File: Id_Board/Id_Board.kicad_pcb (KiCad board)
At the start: 2 copper layers, 130 x 50 mm, 2 parts

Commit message: finished IdBoard
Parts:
- removed REF1: RJ45_Amphenol_RJHSE5380-08, Connector_RJ:RJ45_Amphenol_RJHSE5380-08
- removed REF2: SW_DIP_SPSTx07_Slide_9.78x19.96mm_W7.62mm_P2.54mm, Button_Switch_THT:SW_DIP_SPSTx07_Slide_9.78x19.96mm_W7.62mm_P2.54mm
- added H1: MountingHole, MountingHole:MountingHole_3.2mm_M3, F.Cu at (64.5, 60.0)
- added H2: MountingHole, MountingHole:MountingHole_3.2mm_M3, F.Cu at (175.5, 60.0)
- added H3: MountingHole, MountingHole:MountingHole_3.2mm_M3, F.Cu at (100.0, 70.0)
- added H4: MountingHole, MountingHole:MountingHole_3.2mm_M3, F.Cu at (140.0, 70.0)
- added J1: ~, LCSC:RJ45-TH_HC-WK88-H13-1X8-55QS_1, F.Cu at (120.0, 48.0)
- added J2: Conn_01x02_Pin, Connector_JST:JST_PH_B2B-PH-SM4-TB_1x02-1MP_P2.00mm_Vertical, F.Cu at (74.4, 65.6)
- added J3: Conn_01x02_Pin, Connector_JST:JST_PH_B2B-PH-SM4-TB_1x02-1MP_P2.00mm_Vertical, F.Cu at (164.9, 66.1)
- added R1: 0, Resistor_SMD:R_0603_1608Metric, F.Cu at (163.1, 53.5)
- added R10: 0, Resistor_SMD:R_0603_1608Metric, F.Cu at (121.0, 53.5)
- added R11: 0, Resistor_SMD:R_0603_1608Metric, F.Cu at (124.5, 53.5)
- added R12: 0, Resistor_SMD:R_0603_1608Metric, F.Cu at (122.8, 53.5)
- added R13: 0, Resistor_SMD:R_0603_1608Metric, F.Cu at (107.0, 53.5)
- added R14: 0, Resistor_SMD:R_0603_1608Metric, F.Cu at (110.5, 53.5)
- added R15: 0, Resistor_SMD:R_0603_1608Metric, F.Cu at (108.8, 53.5)
- added R16: 0, Resistor_SMD:R_0603_1608Metric, F.Cu at (93.1, 53.5)
- added R17: 0, Resistor_SMD:R_0603_1608Metric, F.Cu at (96.5, 53.5)
- added R18: 0, Resistor_SMD:R_0603_1608Metric, F.Cu at (94.8, 53.5)
- added R19: 0, Resistor_SMD:R_0603_1608Metric, F.Cu at (79.0, 53.5)
- added R2: 0, Resistor_SMD:R_0603_1608Metric, F.Cu at (166.5, 53.5)
- added R20: 0, Resistor_SMD:R_0603_1608Metric, F.Cu at (82.5, 53.5)
- added R21: 0, Resistor_SMD:R_0603_1608Metric, F.Cu at (80.8, 53.5)
- added R22: 0, Resistor_SMD:R_0603_1608Metric, F.Cu at (64.6, 53.5)
- added R23: 0, Resistor_SMD:R_0603_1608Metric, F.Cu at (68.5, 53.5)
- added R24: 0, Resistor_SMD:R_0603_1608Metric, F.Cu at (66.6, 53.5)
- added R3: 0, Resistor_SMD:R_0603_1608Metric, F.Cu at (164.8, 53.5)
- added R4: 0, Resistor_SMD:R_0603_1608Metric, F.Cu at (149.0, 53.5)
- added R5: 0, Resistor_SMD:R_0603_1608Metric, F.Cu at (152.5, 53.5)
- added R6: 0, Resistor_SMD:R_0603_1608Metric, F.Cu at (150.8, 53.5)
- added R7: 0, Resistor_SMD:R_0603_1608Metric, F.Cu at (135.0, 53.5)
- added R8: 0, Resistor_SMD:R_0603_1608Metric, F.Cu at (138.5, 53.5)
- added R9: 0, Resistor_SMD:R_0603_1608Metric, F.Cu at (136.8, 53.5)
- added SW1: SW_DIP_x08, LCSC:SW-SMD_16P-L20.3-W6.0-P2.54-LS9.3-BL, F.Cu at (120.0, 66.5)
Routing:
- net BoardA: track 0.00 -> 178.6 mm, vias 0 -> 7
- net BoardC: track 0.00 -> 170.7 mm, vias 0 -> 9
- net BoardB: track 0.00 -> 159.8 mm, vias 0 -> 9
- net BoardD: track 0.00 -> 143.2 mm, vias 0 -> 1
- net ParityB: track 0.00 -> 118.5 mm, vias 0 -> 5
- net ParityA: track 0.00 -> 112.7 mm, vias 0 -> 4
- net GND: track 0.00 -> 52.6 mm, vias 0 -> 8
- net Net-(J1-PadE3): track 0.00 -> 7.27 mm
- net Net-(J1-PadC3): track 0.00 -> 7.17 mm
- net Net-(J1-PadH1): track 0.00 -> 7.11 mm
- net Net-(J1-PadH3): track 0.00 -> 7.10 mm
- net Net-(J1-PadF3): track 0.00 -> 7.04 mm
- net Net-(J1-PadD3): track 0.00 -> 7.04 mm
- net Net-(J1-PadB3): track 0.00 -> 7.04 mm
- net Net-(J1-PadA3): track 0.00 -> 7.02 mm
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- added copper zone on B.Cu, net GND
- added copper zone on F.Cu, net GND
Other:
- board size 130 x 50 mm -> 120 x 35 mm

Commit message: Production File generate
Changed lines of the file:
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@@
 				(font
 					(size 1.27 1.27)
+					(thickness 0.15)
 				)
 			)
@@
 				(font
 					(size 1.27 1.27)
+					(thickness 0.15)
 				)
 			)
@@
 				(font
 					(size 1.27 1.27)
+					(thickness 0.15)
 				)
 			)
@@
 		(sheetname "/")
 		(sheetfile "Id_Board.kicad_sch")
-		(units
-			(unit
-				(name "A")
-				(pins "A8" "A7" "A6" "A5" "A4" "A3" "A2" "A1")
-			)
-			(unit
-				(name "B")
-				(pins "B8" "B7" "B6" "B5" "B4" "B3" "B2" "B1")
-			)
-			(unit
-				(name "C")
-				(pins "C8" "C7" "C6" "C5" "C4" "C3" "C2" "C1")
-			)
-			(unit
-				(name "D")
-				(pins "D8" "D7" "D6" "D5" "D4" "D3" "D2" "D1")
-			)
-			(unit
-				(name "E")
-				(pins "E8" "E7" "E6" "E5" "E4" "E3" "E2" "E1")
-			)
-			(unit
-				(name "F")
-				(pins "F8" "F7" "F6" "F5" "F4" "F3" "F2" "F1")
-			)
-			(unit
-				(name "G")
-				(pins "G8" "G7" "G6" "G5" "G4" "G3" "G2" "G1")
-			)
-			(unit
-				(name "H")
-				(pins "H8" "H7" "H6" "H5" "H4" "H3" "H2" "H1")
-			)
-		)
 		(attr through_hole)
 		(duplicate_pad_numbers_are_jumpers no)
@@
 			)
 		)
-		(pad "" thru_hole circle
+		(pad "" np_thru_hole circle
 			(at -54.75 3.86 180)
 			(size 3.2 3.2)
 			(drill 3.2)
 			(layers "*.Cu" "*.Mask")
-			(remove_unused_layers no)
 		)
-		(pad "" thru_hole circle
+		(pad "" np_thru_hole circle
 			(at 54.75 3.86 180)
 			(size 3.2 3.2)
 			(drill 3.2)
 			(layers "*.Cu" "*.Mask")
-			(remove_unused_layers no)
 		)
 		(pad "A1" thru_hole circle
@@
 				(font
 					(size 1.27 1.27)
+					(thickness 0.15)
 				)
 			)
@@
 				(font
 					(size 1.27 1.27)
+					(thickness 0.15)
 				)
 			)
@@
 				(font
 					(size 1.27 1.27)
+					(thickness 0.15)
 				)
 			)
@@
 				(font
 					(size 1.27 1.27)
+					(thickness 0.15)
 				)
 			)
@@
 				(font
 					(size 1.27 1.27)
+					(thickness 0.15)
 				)
 			)
@@
 				(font
 					(size 1.27 1.27)
+					(thickness 0.15)
 				)
 			)
@@
 				(font
 					(size 1.27 1.27)
+					(thickness 0.15)
 				)
 			)
@@
 				(font
 					(size 1.27 1.27)
+					(thickness 0.15)
 				)
 			)
@@
 				(font
 					(size 1.27 1.27)
+					(thickness 0.15)
 				)
 			)
@@
 				(font
 					(size 1.27 1.27)
+					(thickness 0.15)
 				)
 			)
@@
 				(font
 					(size 1.27 1.27)
+					(thickness 0.15)
 				)
 			)
@@
 				(font
 					(size 1.27 1.27)
+					(thickness 0.15)
 				)
 			)
@@
 				(font
 					(size 1.27 1.27)
+					(thickness 0.15)
 				)
 			)
@@
 				(font
 					(size 1.27 1.27)
+					(thickness 0.15)
 				)
 			)
@@
 				(font
 					(size 1.27 1.27)
+					(thickness 0.15)
 				)
 			)
@@
 				(font
 					(size 1.27 1.27)
+					(thickness 0.15)
 				)
 			)
@@
 				(font
 					(size 1.27 1.27)
+					(thickness 0.15)
 				)
 			)
@@
 				(font
 					(size 1.27 1.27)
+					(thickness 0.15)
 				)
 			)
@@
 				(font
 					(size 1.27 1.27)
+					(thickness 0.15)
 				)
 			)
@@
 				(font
 					(size 1.27 1.27)
+					(thickness 0.15)
 				)
 			)
@@
 				(font
 					(size 1.27 1.27)
+					(thickness 0.15)
 				)
 			)

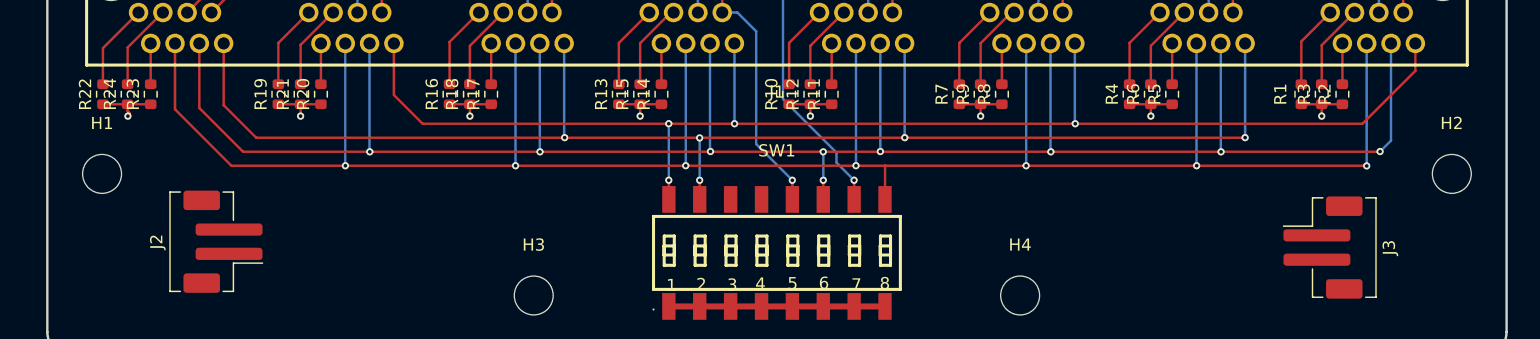
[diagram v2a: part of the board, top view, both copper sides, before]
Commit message: prettify silkscreen
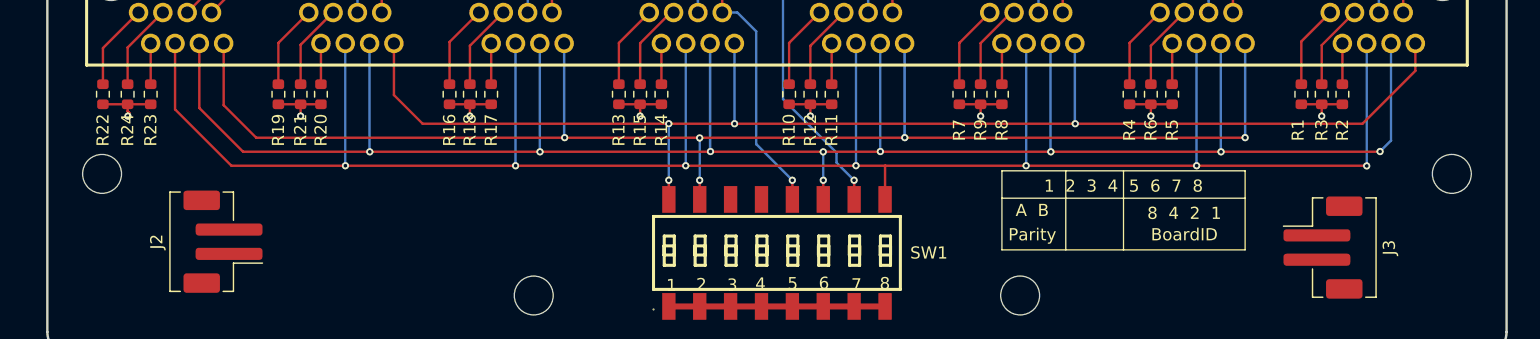
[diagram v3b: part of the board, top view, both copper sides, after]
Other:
- board text added: "1 2 3 4 5 6 7 8"
- board text added: "8 4 2 1"
- board text added: "A B"
- board text added: "BoardID"
- board text added: "Parity"
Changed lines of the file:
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@@
 		(tags "resistor")
 		(property "Reference" "R22"
-			(at 0 -1.43 90)
+			(at -2.95 0 90)
 			(layer "F.SilkS")
 			(effects
@@
 		(tags "resistor")
 		(property "Reference" "R24"
-			(at 0 -1.43 90)
+			(at -2.95 0 90)
 			(layer "F.SilkS")
 			(effects
@@
 		(tags "resistor")
 		(property "Reference" "R17"
-			(at 0 -1.43 90)
+			(at -2.95 0 90)
 			(layer "F.SilkS")
 			(effects
@@
 			(at 0 -4.15 0)
 			(layer "F.SilkS")
+			(hide yes)
 			(effects
 				(font
@@
 			(at 0 -5.27 0)
 			(layer "F.SilkS")
+			(hide yes)
 			(effects
 				(font
@@
 		(tags "resistor")
 		(property "Reference" "R15"
-			(at 0 -1.43 90)
+			(at -2.95 0 90)
 			(layer "F.SilkS")
 			(effects
@@
 		(tags "resistor")
 		(property "Reference" "R18"
-			(at 0 -1.43 90)
+			(at -2.95 0 90)
 			(layer "F.SilkS")
 			(effects
@@
 		(tags "resistor")
 		(property "Reference" "R19"
-			(at 0 -1.43 90)
+			(at -2.95 0 90)
 			(layer "F.SilkS")
 			(effects
@@
 			(at 0 -4.15 0)
 			(layer "F.SilkS")
+			(hide yes)
 			(effects
 				(font
@@
 			(at 0 -4.15 0)
 			(layer "F.SilkS")
+			(hide yes)
 			(effects
 				(font
@@
 		(tags "resistor")
 		(property "Reference" "R14"
-			(at 0 -1.43 90)
+			(at -2.95 0 90)
 			(layer "F.SilkS")
 			(effects
@@
 		(tags "resistor")
 		(property "Reference" "R2"
-			(at 0 -1.43 90)
+			(at -2.95 0 90)
 			(layer "F.SilkS")
 			(effects
@@
 		(tags "resistor")
 		(property "Reference" "R20"
-			(at 0 -1.43 90)
+			(at -2.95 0 90)
 			(layer "F.SilkS")
 			(effects
@@
 		(tags "resistor")
 		(property "Reference" "R10"
-			(at 0 -1.43 90)
+			(at -2.95 0 90)
 			(layer "F.SilkS")
 			(effects
@@
 		(tags "resistor")
 		(property "Reference" "R11"
-			(at 0 -1.43 90)
+			(at -2.95 0 90)
 			(layer "F.SilkS")
 			(effects
@@
 		(tags "resistor")
 		(property "Reference" "R23"
-			(at 0 -1.43 90)
+			(at -2.95 0 90)
 			(layer "F.SilkS")
 			(effects
@@
 		(tags "resistor")
 		(property "Reference" "R1"
-			(at 0 -1.7 90)
+			(at -2.95 -0.27 90)
 			(layer "F.SilkS")
 			(effects
@@
 		(tags "resistor")
 		(property "Reference" "R5"
-			(at 0 -1.43 90)
+			(at -2.95 0 90)
 			(layer "F.SilkS")
 			(effects
@@
 		(tags "resistor")
 		(property "Reference" "R3"
-			(at 0 -1.43 90)
+			(at -2.95 0 90)
 			(layer "F.SilkS")
 			(effects
@@
 		(tags "resistor")
 		(property "Reference" "R4"
-			(at 0 -1.43 90)
+			(at -2.95 0 90)
 			(layer "F.SilkS")
 			(effects
@@
 		(tags "resistor")
 		(property "Reference" "R8"
-			(at 0 -1.43 90)
+			(at -2.95 0 90)
 			(layer "F.SilkS")
 			(effects
@@
 		(tags "resistor")
 		(property "Reference" "R13"
-			(at 0 -1.43 90)
+			(at -2.95 0 90)
 			(layer "F.SilkS")
 			(effects
@@
 			(at 0 -4.15 0)
 			(layer "F.SilkS")
+			(hide yes)
 			(effects
 				(font
@@
 		(tags "resistor")
 		(property "Reference" "R9"
-			(at 0 -1.43 90)
+			(at -2.95 0 90)
 			(layer "F.SilkS")
 			(effects
@@
 		(tags "resistor")
 		(property "Reference" "R16"
-			(at 0 -1.43 90)
+			(at -2.95 0 90)
 			(layer "F.SilkS")
 			(effects
@@
 		(tags "resistor")
 		(property "Reference" "R12"
-			(at 0 -1.43 90)
+			(at -2.95 0 90)
 			(layer "F.SilkS")
 			(effects
@@
 		(at 120 66.5)
 		(property "Reference" "SW1"
-			(at 0 -8.4 0)
+			(at 12.5 0 0)
 			(layer "F.SilkS")
 			(effects
@@
 		(tags "resistor")
 		(property "Reference" "R6"
-			(at 0 -1.43 90)
+			(at -2.95 0 90)
 			(layer "F.SilkS")
 			(effects
@@
 		(tags "resistor")
 		(property "Reference" "R7"
-			(at 0 -1.43 90)
+			(at -2.95 0 90)
 			(layer "F.SilkS")
 			(effects
@@
 		(tags "resistor")
 		(property "Reference" "R21"
-			(at 0 -1.43 90)
+			(at -2.95 0 90)
 			(layer "F.SilkS")
 			(effects
@@
 		)
 	)
+	(gr_rect
+		(start 138.5 59.75)
+		(end 158.5 66.25)
+		(stroke
+			(width 0.1)
+			(type default)
+		)
+		(fill no)
+		(layer "F.SilkS")
+	)
+	(gr_line
+		(start 138.5 62)
+		(end 158.5 62)
+		(stroke
+			(width 0.1)
+			(type default)
+		)
+		(layer "F.SilkS")
+	)
+	(gr_line
+		(start 143.75 59.75)
+		(end 143.75 66.25)
+		(stroke
+			(width 0.1)
+			(type default)
+		)
+		(layer "F.SilkS")
+	)
+	(gr_line
+		(start 148.5 59.75)
+		(end 148.5 66.25)
+		(stroke
+			(width 0.1)
+			(type default)
+		)
+		(layer "F.SilkS")
+	)
 	(gr_line
 		(start 60 42)
@@
 		(layer "Edge.Cuts")
 	)
+	(gr_text "A  B"
+		(at 141 63 0)
+		(layer "F.SilkS")
+		(effects
+			(font
+				(size 1 1)
+				(thickness 0.1)
+			)
+		)
+	)
+	(gr_text "Parity"
+		(at 141 65 0)
+		(layer "F.SilkS")
+		(effects
+			(font
+				(size 1 1)
+				(thickness 0.1)
+			)
+		)
+	)
+	(gr_text "8  4  2  1"
+		(at 153.5 63.240579 0)
+		(layer "F.SilkS")
+		(effects
+			(font
+				(size 1 1)
+				(thickness 0.1)
+			)
+		)
+	)
+	(gr_text "BoardID"
+		(at 153.5 65 0)
+		(layer "F.SilkS")
+		(effects
+			(font
+				(size 1 1)
+				(thickness 0.1)
+			)
+		)
+	)
+	(gr_text "1  2  3  4  5  6  7  8"
+		(at 148.5 61 0)
+		(layer "F.SilkS")
+		(effects
+			(font
+				(size 1 1)
+				(thickness 0.15)
+			)
+		)
+	)
 	(segment
